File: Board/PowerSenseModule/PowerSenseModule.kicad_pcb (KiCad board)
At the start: 2 copper layers, 130 x 65 mm, 62 parts, among them J1 Conn_01x06_Male, J3 Programming Header, J4 Conn_01x02_Male, U1 TPS82150, U2 NCV2007x, U3 dsPIC33EV32GM102, U4 MCP2542FDxMF, Y1 25 MHz

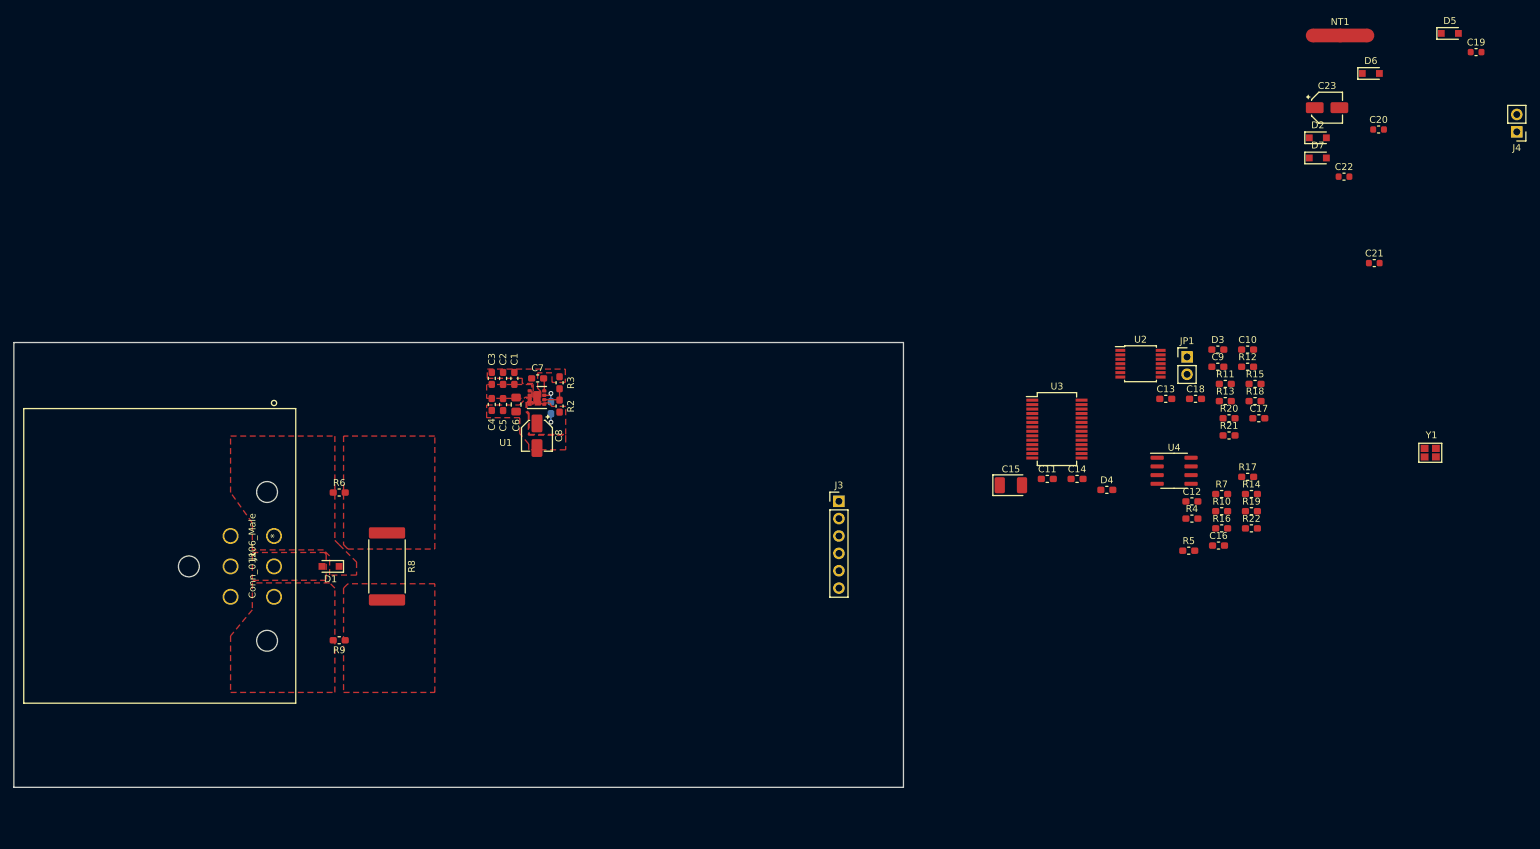
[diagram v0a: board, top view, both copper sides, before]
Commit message: Laid out crystal and grouped together components
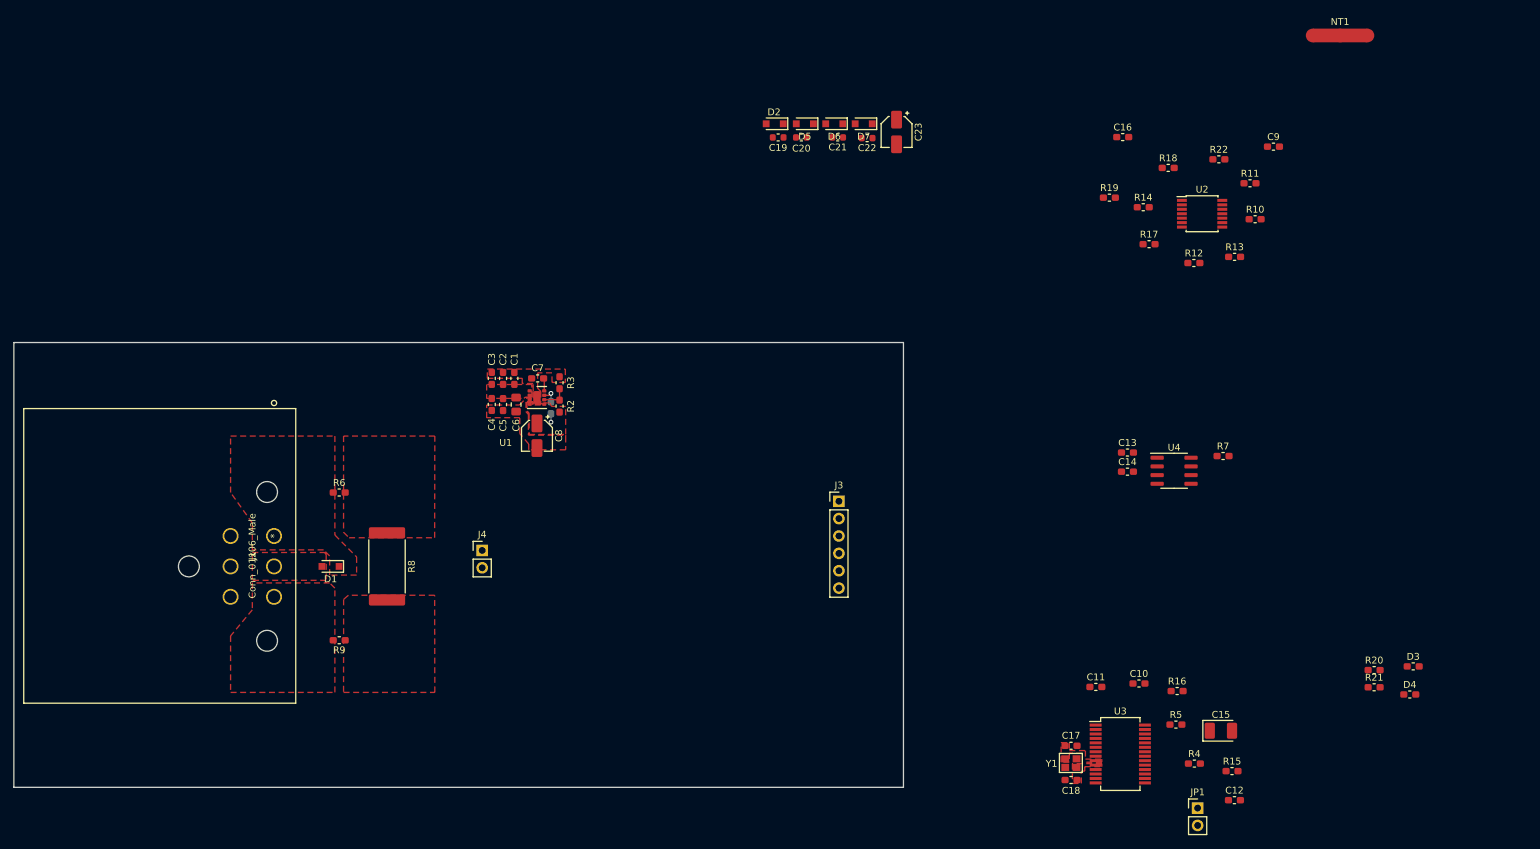
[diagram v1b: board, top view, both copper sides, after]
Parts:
- moved J4 163.1 mm to (118.0, 106.2), turned to 0 degrees
- moved C19 102.7 mm to (161.3, 45.9), turned to 180 degrees
- moved D5 95.2 mm to (165.2, 43.9), turned to 180 degrees
- moved C20 84.4 mm to (164.7, 45.9)
- moved C21 80.5 mm to (170.0, 45.9), turned to 180 degrees
- moved D2 79.4 mm to (160.8, 43.9), turned to 180 degrees
- moved D6 78.8 mm to (169.5, 43.9), turned to 180 degrees
- moved C22 69.9 mm to (174.3, 46.0), turned to 180 degrees
- moved D7 66.5 mm to (173.8, 43.9), turned to 180 degrees
- moved JP1 65.9 mm to (222.6, 143.9)
- moved Y1 65.9 mm to (205.4, 136.2), turned to 180 degrees
- moved C23 63.0 mm to (178.6, 45.1), turned to 270 degrees
- moved C16 61.3 mm to (211.7, 45.9)
- moved C18 58.6 mm to (204.1, 139.8), turned to 180 degrees
- moved R15 56.7 mm to (227.6, 138.5)
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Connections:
- Y1 pad 4: GNDA -> (no net)
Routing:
- added copper zone on F.Cu, net /MCU and CAN/OSC1
- added copper zone on F.Cu, net /MCU and CAN/OSC2

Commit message: Changed crystal gnd net and working on layout
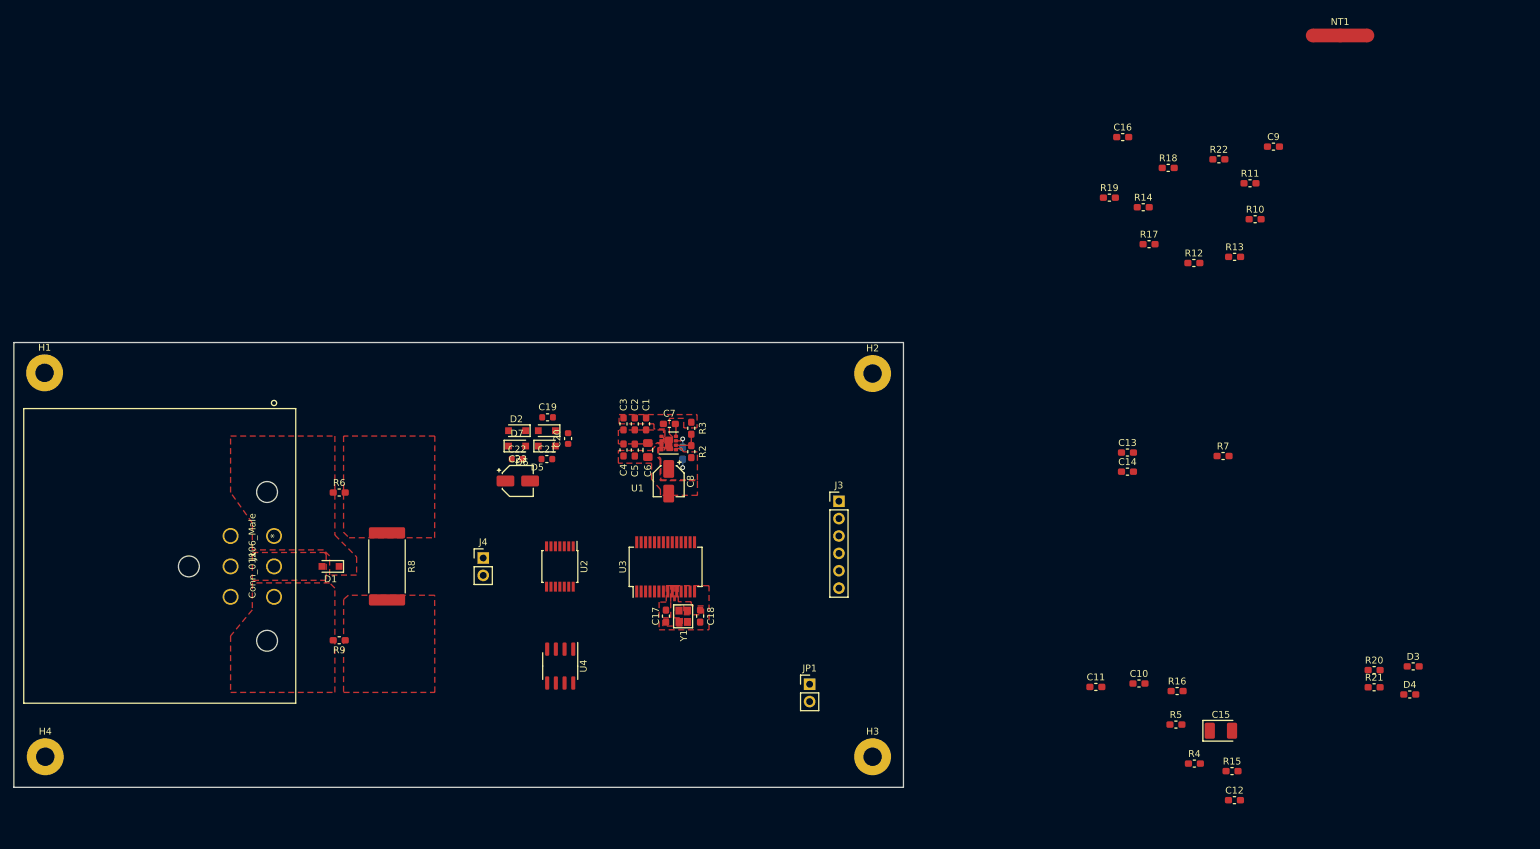
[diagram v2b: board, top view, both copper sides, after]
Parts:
- added H1: MountingHole_Pad, MountingHole:MountingHole_2.7mm_M2.5_Pad, F.Cu at (54.1, 80.3)
- added H2: MountingHole_Pad, MountingHole:MountingHole_2.7mm_M2.5_Pad, F.Cu at (175.1, 80.4)
- added H3: MountingHole_Pad, MountingHole:MountingHole_2.7mm_M2.5_Pad, F.Cu at (175.1, 136.4)
- added H4: MountingHole_Pad, MountingHole:MountingHole_2.7mm_M2.5_Pad, F.Cu at (54.2, 136.4)
- moved U2 107.1 mm to (129.4, 108.6), turned to 270 degrees
- moved U4 94.1 mm to (129.4, 123.2), turned to 270 degrees
- moved C23 75.3 mm to (123.2, 96.1), turned to 0 degrees
- moved U3 71.9 mm to (144.9, 108.7), turned to 90 degrees
- moved C22 69.4 mm to (123.2, 92.9), turned to 0 degrees
- moved D7 69.2 mm to (123.2, 91.0), turned to 0 degrees
- moved C21 63.4 mm to (127.5, 92.9), turned to 0 degrees
- moved D6 63.1 mm to (127.5, 91.0), turned to 0 degrees
- moved Y1 62.9 mm to (146.3, 114.6), turned to 270 degrees
- moved C17 62.2 mm to (144.9, 115.9), turned to 90 degrees
- moved JP1 59.5 mm to (165.9, 125.8)
- moved C18 59.3 mm to (149.9, 115.9), turned to 270 degrees
- moved D5 58.6 mm to (127.5, 88.8)
- moved D2 58.6 mm to (123.2, 88.8)
- moved C20 55.7 mm to (130.6, 89.9), turned to 270 degrees
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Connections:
- C17 pad 2: GNDA -> GNDD
- C18 pad 2: GNDA -> GNDD
- Y1 pad 2: GNDA -> GNDD
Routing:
- added copper zone on F.Cu, net GNDD
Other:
- net class Default: clearance 0.2 -> 0.14
- net class JLC Min added: clearance 0.9, trace_width 0.9, via_dia 0.45, via_drill 0.2
- rule trace_clearance: 0.2 -> 0.14

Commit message: layout 0.01
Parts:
- added C24: 0.01uF, Capacitor_SMD:C_0603_1608Metric_Pad1.05x0.95mm_HandSolder, B.Cu at (129.5, 109.5)
- NT1, R10, R11, R19: moved to B.Cu
- moved NT1 132.7 mm to (135.6, 108.2), turned to 270 degrees
- moved C9 117.8 mm to (137.9, 116.0), turned to 270 degrees
- moved R11 116.3 mm to (127.8, 107.7), turned to 90 degrees
- moved R10 116.1 mm to (126.1, 107.7), turned to 90 degrees
- moved R13 112.4 mm to (127.7, 114.0)
- moved R22 110.5 mm to (134.0, 110.7), turned to 270 degrees
- moved R7 108.1 mm to (124.5, 128.8), turned to 270 degrees
- moved R12 103.6 mm to (131.2, 114.0)
- moved C16 99.8 mm to (135.8, 110.7), turned to 270 degrees
- moved R18 98.9 mm to (134.5, 102.8)
- moved R14 98.8 mm to (136.1, 116.0), turned to 270 degrees
- moved R19 94.7 mm to (131.2, 107.7), turned to 270 degrees
- moved D3 93.3 mm to (161.0, 129.2), turned to 180 degrees
- moved D4 92.7 mm to (161.0, 131.0), turned to 180 degrees
- moved R20 91.2 mm to (157.4, 129.2)
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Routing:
- net (no net): vias 0 -> 1

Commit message: layout 0.02
most power is routed
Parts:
- C24: moved to F.Cu
- moved D4 35.9 mm to (155.9, 95.5)
- moved R21 35.9 mm to (152.3, 95.5)
- moved D3 32.3 mm to (155.9, 97.3)
- moved R20 32.3 mm to (152.3, 97.3), turned to 180 degrees
- moved J3 20.5 mm to (156.8, 114.6), turned to 180 degrees
- moved R18 15.3 mm to (121.2, 110.3), turned to 90 degrees
- moved R17 14.4 mm to (121.2, 106.7), turned to 90 degrees
- moved C24 8.37 mm to (123.8, 103.3), turned to 180 degrees
- moved R5 4.55 mm to (137.1, 115.9), turned to 90 degrees
- moved C16 3.60 mm to (132.2, 110.7)
- moved C13 3.60 mm to (149.1, 106.8)
- moved C14 3.60 mm to (149.1, 110.2)
- moved C15 3.60 mm to (143.8, 101.8)
- moved C17 3.60 mm to (141.3, 115.9)
- moved C18 3.60 mm to (146.3, 115.9)
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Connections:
- C20 pad 2: GNDA -> GND
- C22 pad 2: GNDA -> GND
- C23 pad 2: GNDA -> GND
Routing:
- net +5V: track 1.22 -> 111.5 mm
- net GNDA: track 0.00 -> 16.1 mm
- net Net-(J4-Pad2): track 0.00 -> 12.5 mm
- net Net-(J4-Pad1): track 0.00 -> 12.4 mm
- net Net-(R10-Pad2): vias 0 -> 1
- net (no net): vias 1 -> 0
- added copper zone on B.Cu, net GND
- added copper zone on B.Cu, net GNDA
- added copper zone on F.Cu, net GNDA
- added copper zone on F.Cu, net Net-(C19-Pad1)
- added copper zone on F.Cu, net Net-(C20-Pad1)
- added copper zone on F.Cu, net Net-(C21-Pad1)
- added copper zone on F.Cu, net VS
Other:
- net class Default: trace_width 0.1524 -> 0.25
- net class Default - thick trace added: clearance 0.4, trace_width 0.25, via_dia 0.7, via_drill 0.4
- net class JLC Min: trace_width 0.9 -> 0.09

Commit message: layout 0.03
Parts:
- moved JP1 21.2 mm to (156.8, 119.8), turned to 0 degrees
- moved C12 15.1 mm to (137.1, 119.5), turned to 90 degrees
- moved R16 11.4 mm to (141.9, 120.5)
- moved R15 10.2 mm to (145.5, 120.5), turned to 180 degrees
- moved R7 8.63 mm to (121.7, 120.7)
- moved U4 8.21 mm to (129.1, 120.5)
- moved C11 6.60 mm to (133.6, 119.5)
- moved C10 6.60 mm to (135.3, 119.5)
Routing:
- net /MCU and CAN/MCLR: track 0.00 -> 31.6 mm
- net /MCU and CAN/LED2: track 0.00 -> 20.3 mm
- net /MCU and CAN/LED1: track 0.00 -> 17.7 mm
- net +5V: track 111.5 -> 124.6 mm
- net Net-(C12-Pad1): track 0.00 -> 12.6 mm
- net VS: track 0.00 -> 12.4 mm
- net GNDA: track 16.1 -> 7.35 mm
- net Net-(R22-Pad2): track 0.00 -> 3.21 mm
- net Net-(C15-Pad1): track 0.00 -> 3.20 mm
- net GNDD: track 0.00 -> 3.20 mm
- net Net-(R5-Pad2): track 0.00 -> 2.78 mm
- net Net-(D4-Pad2): track 0.00 -> 1.85 mm
- net Net-(D3-Pad2): track 0.00 -> 1.85 mm
